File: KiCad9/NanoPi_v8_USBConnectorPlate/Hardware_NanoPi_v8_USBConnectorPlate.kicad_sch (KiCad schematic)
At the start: 17 parts, among them J10 Conn_01x04, J11 Conn_01x02, J12 Conn_01x02, J2 USB_Host_Data_02x02, J3 USB_Host_Data_02x02, J4 USB_Power_02x02, J5 Conn_01x03, J6 Conn_01x09, J8 Conn_01x09, U1 USBLC6-2P6, U2 USBLC6-2P6, U3 USBLC6-2P6

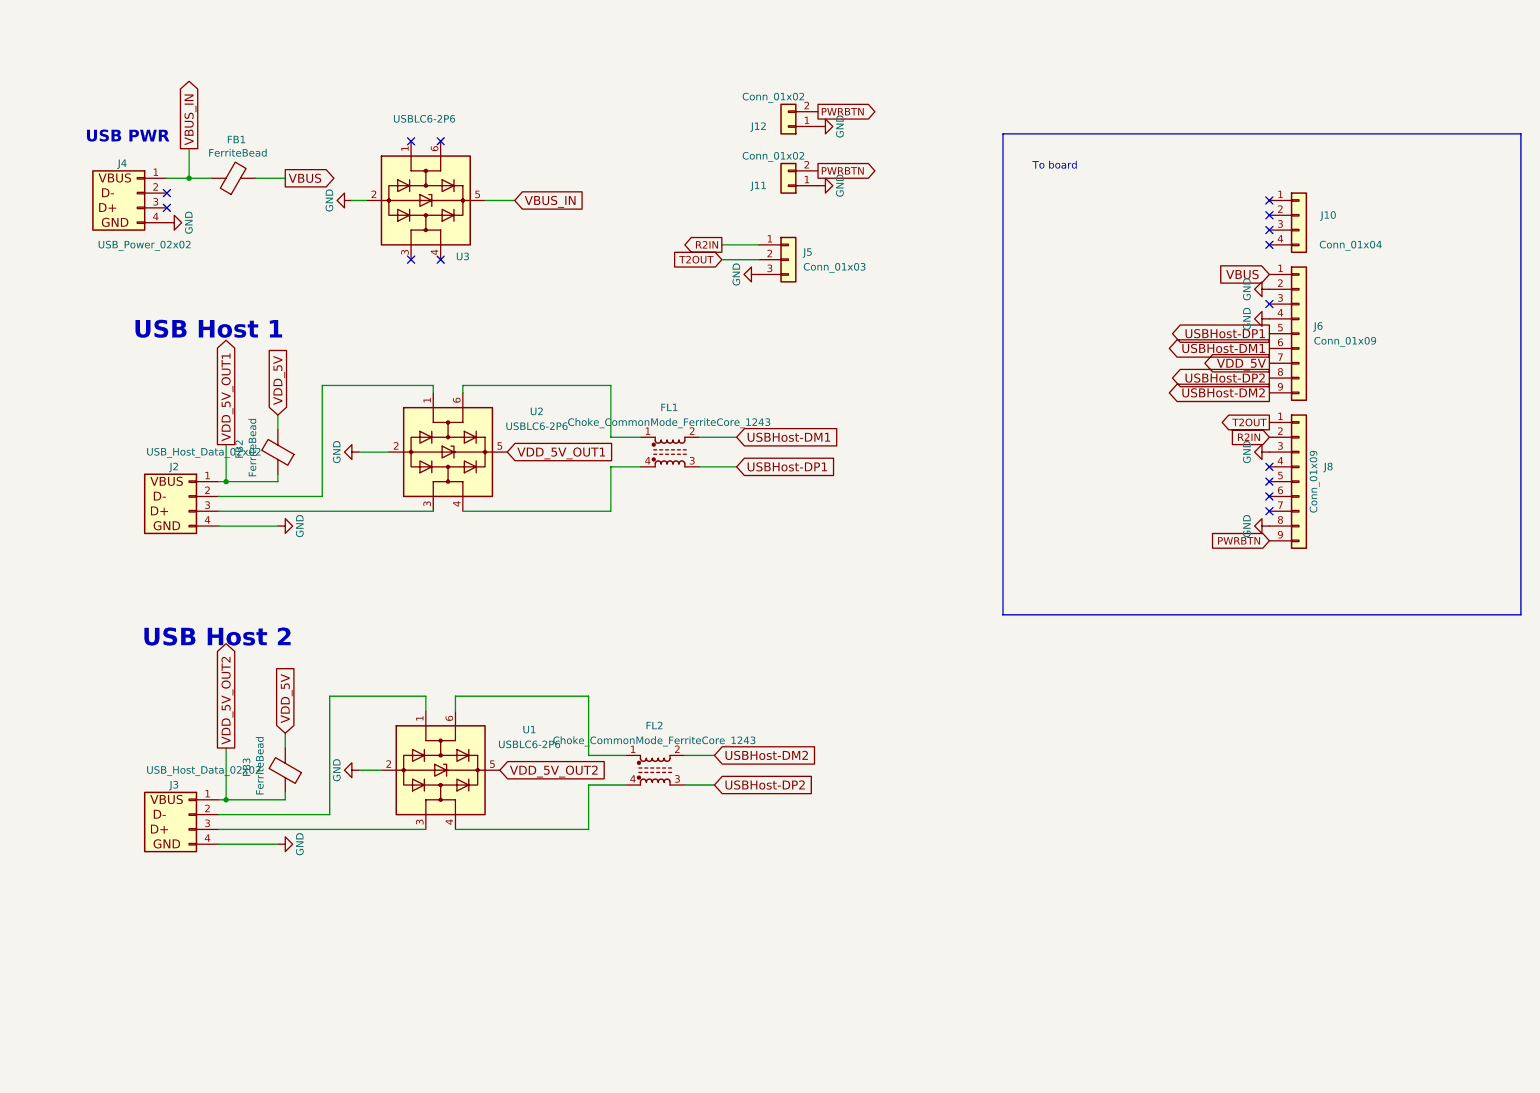
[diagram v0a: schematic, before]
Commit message: add bom
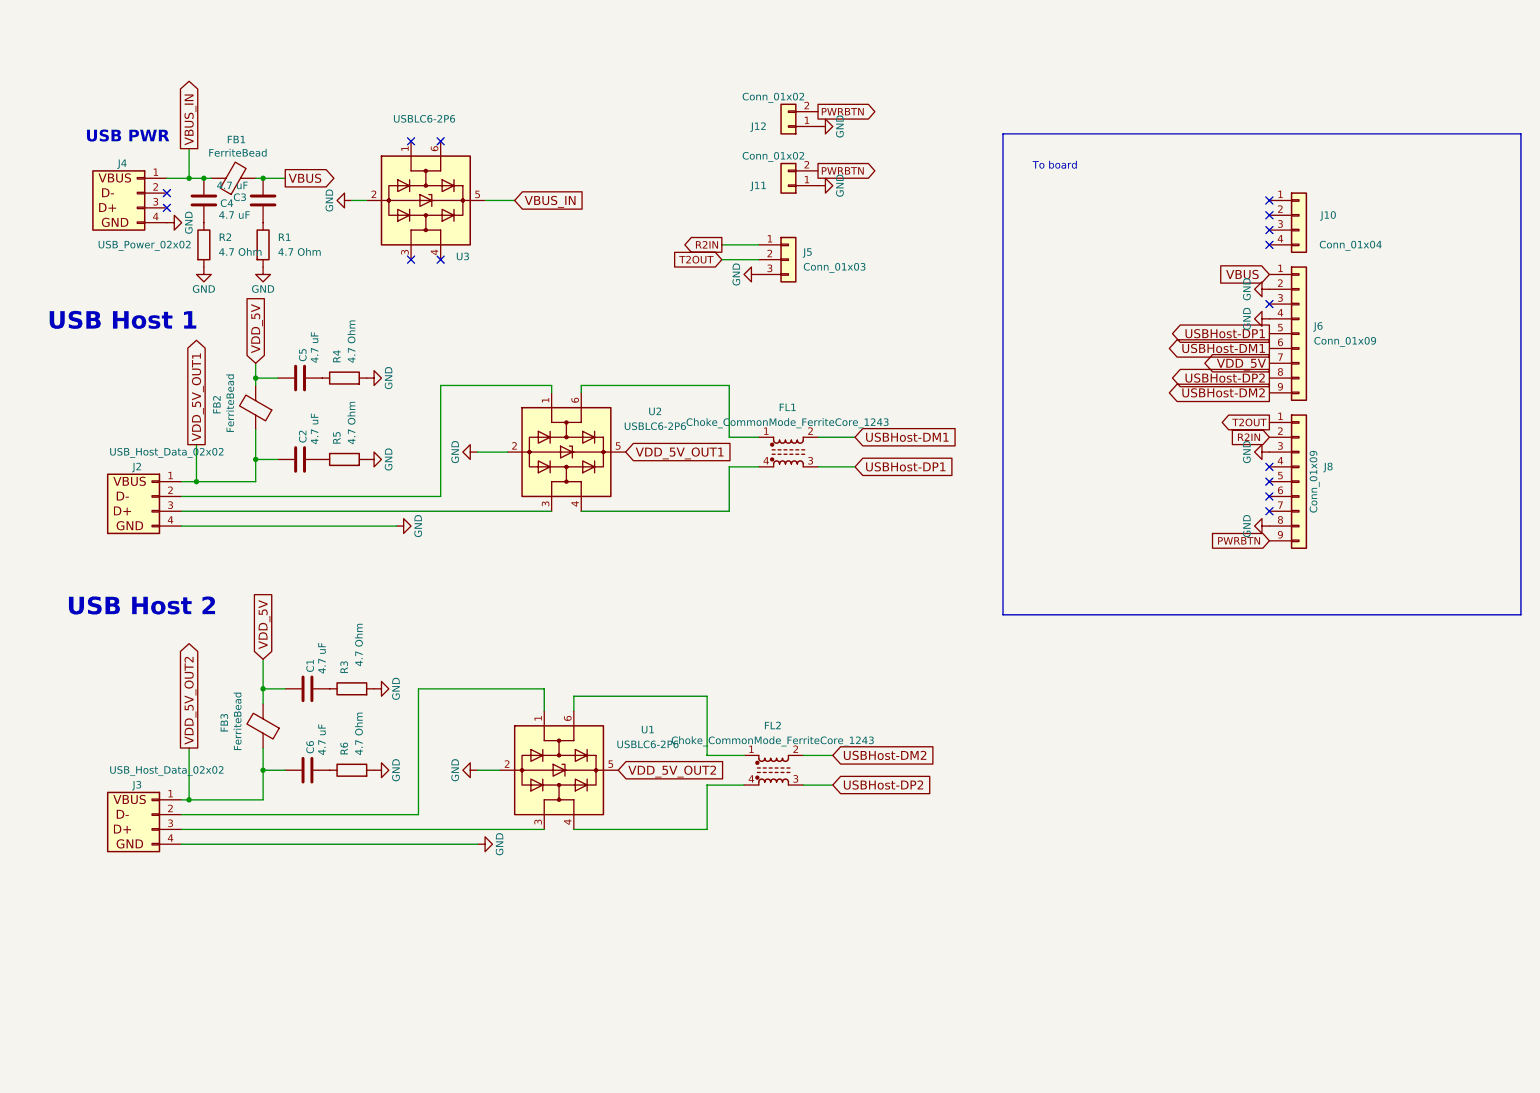
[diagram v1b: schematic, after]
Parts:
- added C1, C2, C3, C4, C5, C6: 4.7 uF, Capacitor_SMD:C_0402_1005Metric, symbol Device:C
- added R1, R2, R3, R4, R5, R6: 4.7 Ohm, Resistor_SMD:R_0603_1608Metric, symbol Device:R
- FB1, FB2: LCSC (none) -> C16902; LCSC Part # (none) -> C16902
- FB3: LCSC (none) -> C16902; LCSC Part # (none) -> C16902; Package (none) -> 1206; PartNumber (none) -> BLM31PG601SN1
- FL1, FL2: LCSC (none) -> C2980700; Package (none) -> SMD-4P,1.2x2mm; PartNumber (none) -> SDCW2012L-2-900TF
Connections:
- net GND: now also R1.2, R2.2, R3.2, R4.2, R5.2, R6.2
- net VBUS: now also C3.2
- net VBUS_IN: now also C4.1
- net VDD_5V: now also C1.1, C5.1
- net VDD_5V_OUT1: now also C2.1
- net VDD_5V_OUT2: now also C6.1
- new net: C5.2, R4.1
- new net: C4.2, R2.1
- new net: C3.1, R1.1
- new net: C1.2, R3.1
- new net: C2.2, R5.1
- new net: C6.2, R6.1
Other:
- moved on the sheet: FB2, FB3, FL1, J2, J3, U1, U2

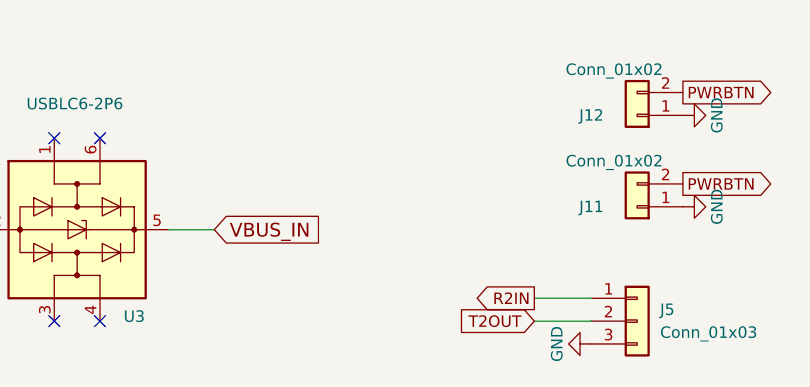
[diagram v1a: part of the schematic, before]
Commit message: add 3d of wifiboard
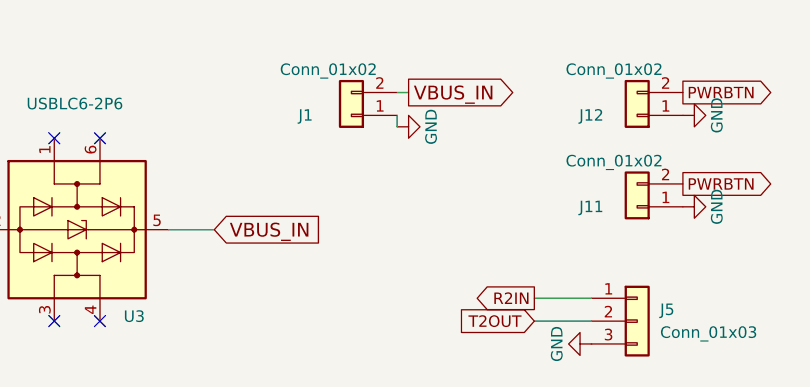
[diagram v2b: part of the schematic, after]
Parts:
- added J1: Conn_01x02, Connector_PinHeader_2.54mm:PinHeader_1x02_P2.54mm_Horizontal, symbol Connector_Generic:Conn_01x02
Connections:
- net GND: now also J1.1 (Pin_1)
- net VBUS_IN: now also J1.2 (Pin_2)
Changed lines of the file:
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@@
 	(wire
 		(pts
+			(xy 115.57 33.02) (xy 115.57 31.75)
+		)
+		(stroke
+			(width 0)
+			(type default)
+		)
+	)
+	(wire
+		(pts
 			(xy 130.81 52.07) (xy 137.16 52.07)
 		)
@@
 	(wire
 		(pts
+			(xy 116.84 29.21) (xy 115.57 29.21)
+		)
+		(stroke
+			(width 0)
+			(type default)
+		)
+	)
+	(wire
+		(pts
 			(xy 130.81 54.61) (xy 137.16 54.61)
 		)
@@
 		)
 	)
+	(global_label "VBUS_IN"
+		(shape output)
+		(at 116.84 29.21 0)
+		(fields_autoplaced yes)
+		(effects
+			(font
+				(size 1.524 1.524)
+			)
+			(justify left)
+		)
+		(property "Intersheetrefs" "${INTERSHEET_REFS}"
+			(at 129.7834 29.21 0)
+			(effects
+				(font
+					(size 1.27 1.27)
+				)
+				(justify left)
+				(hide yes)
+			)
+		)
+	)
 	(global_label "USBHost-DM2"
 		(shape input)
@@
 	(symbol
 		(lib_id "power:GND")
+		(at 115.57 33.02 90)
+		(unit 1)
+		(exclude_from_sim no)
+		(in_bom yes)
+		(on_board yes)
+		(dnp no)
+		(property "Reference" "#PWR020"
+			(at 121.92 33.02 0)
+			(effects
+				(font
+					(size 1.27 1.27)
+				)
+				(hide yes)
+			)
+		)
+		(property "Value" "GND"
+			(at 119.38 33.02 0)
+			(effects
+				(font
+					(size 1.27 1.27)
+				)
+			)
+		)
+		(property "Footprint" ""
+			(at 115.57 33.02 0)
+			(effects
+				(font
+					(size 1.27 1.27)
+				)
+				(hide yes)
+			)
+		)
+		(property "Datasheet" ""
+			(at 115.57 33.02 0)
+			(effects
+				(font
+					(size 1.27 1.27)
+				)
+				(hide yes)
+			)
+		)
+		(property "Description" ""
+			(at 115.57 33.02 0)
+			(effects
+				(font
+					(size 1.27 1.27)
+				)
+				(hide yes)
+			)
+		)
+		(pin "1"
+		)
+		(instances
+			(project "Hardware_NanoPi_v8_USBConnectorPlate"
+				(path "/9af3723b-dbaa-4340-b307-945f921ae404"
+					(reference "#PWR020")
+					(unit 1)
+				)
+			)
+		)
+	)
+	(symbol
+		(lib_id "power:GND")
 		(at 71.12 142.24 90)
 		(unit 1)
@@
 					(unit 1)
 				)
+			)
+		)
+	)
+	(symbol
+		(lib_id "Connector_Generic:Conn_01x02")
+		(at 110.49 31.75 180)
+		(unit 1)
+		(exclude_from_sim no)
+		(in_bom yes)
+		(on_board yes)
+		(dnp no)
+		(property "Reference" "J1"
+			(at 105.41 31.75 0)
+			(effects
+				(font
+					(size 1.27 1.27)
+				)
+			)
+		)
+		(property "Value" "Conn_01x02"
+			(at 107.95 26.67 0)
+			(effects
+				(font
+					(size 1.27 1.27)
+				)
+			)
+		)
+		(property "Footprint" "Connector_PinHeader_2.54mm:PinHeader_1x02_P2.54mm_Horizontal"
+			(at 110.49 31.75 0)
+			(effects
+				(font
+					(size 1.27 1.27)
+				)
+				(hide yes)
+			)
+		)
+		(property "Datasheet" "~"
+			(at 110.49 31.75 0)
+			(effects
+				(font
+					(size 1.27 1.27)
+				)
+				(hide yes)
+			)
+		)
+		(property "Description" ""
+			(at 110.49 31.75 0)
+			(effects
+				(font
+					(size 1.27 1.27)
+				)
+				(hide yes)
+			)
+		)
+		(pin "1"
+		)
+		(pin "2"
+		)
+		(instances
+			(project "Hardware_NanoPi_v8_USBConnectorPlate"
+				(path "/9af3723b-dbaa-4340-b307-945f921ae404"
+					(reference "J1")
+					(unit 1)
+				)

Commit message: etc
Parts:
- removed FL1, FL2: Choke_CommonMode_FerriteCore_1243, WiRoc:0805_CommonModeChoke, symbol Filter:Choke_CommonMode_FerriteCore_1243
- added FL3, FL4: Choke_CommonMode_FerriteCore_1423, WiRoc:0805_CommonModeChoke_1423, symbol Filter:Choke_CommonMode_FerriteCore_1423
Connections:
- net USBHost-DM1: now also FL3.4
- net USBHost-DM2: now also FL4.4
- net USBHost-DP1: now also FL3.3
- net USBHost-DP2: now also FL4.3
- net at U1.6 (I/O1): now also FL4.1
- net at U1.4 (I/O2): now also FL4.2
- net at U2.6 (I/O1): now also FL3.1
- net at U2.4 (I/O2): now also FL3.2
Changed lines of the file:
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@@
 	)
 	(symbol
-		(lib_id "Filter:Choke_CommonMode_FerriteCore_1243")
-		(at 139.7 142.24 0)
-		(unit 1)
-		(exclude_from_sim no)
-		(in_bom yes)
-		(on_board yes)
-		(dnp no)
-		(fields_autoplaced yes)
-		(property "Reference" "FL2"
-			(at 139.573 134.62 0)
-			(effects
-				(font
-					(size 1.27 1.27)
-				)
-			)
-		)
-		(property "Value" "Choke_CommonMode_FerriteCore_1243"
-			(at 139.573 137.16 0)
-			(effects
-				(font
-					(size 1.27 1.27)
-				)
-			)
-		)
-		(property "Footprint" "WiRoc:0805_CommonModeChoke"
-			(at 139.7 148.59 0)
-			(effects
-				(font
-					(size 1.27 1.27)
-				)
-				(hide yes)
-			)
-		)
-		(property "Datasheet" "https://jlcpcb.com/api/file/downloadByFileSystemAccessId/8590903681308958720"
-			(at 139.7 150.495 0)
-			(effects
-				(font
-					(size 1.27 1.27)
-				)
-				(hide yes)
-			)
-		)
-		(property "Description" "Generic common-mode choke, ferrite core, 1243 pin order"
-			(at 143.764 143.002 0)
-			(effects
-				(font
-					(size 1.27 1.27)
-				)
-				(hide yes)
-			)
-		)
-		(property "PartNumber" "SDCW2012L-2-900TF"
-			(at 139.7 142.24 0)
-			(effects
-				(font
-					(size 1.27 1.27)
-				)
-				(hide yes)
-			)
-		)
-		(property "LCSC" "C2980700"
-			(at 139.7 142.24 0)
-			(effects
-				(font
-					(size 1.27 1.27)
-				)
-				(hide yes)
-			)
-		)
-		(property "Package" "SMD-4P,1.2x2mm"
-			(at 139.7 142.24 0)
-			(effects
-				(font
-					(size 1.27 1.27)
-				)
-				(hide yes)
-			)
-		)
-		(pin "4"
-		)
-		(pin "2"
-		)
-		(pin "1"
-		)
-		(pin "3"
-		)
-		(instances
-			(project "Hardware_NanoPi_v8_USBConnectorPlate"
-				(path "/9af3723b-dbaa-4340-b307-945f921ae404"
-					(reference "FL2")
-					(unit 1)
-				)
-			)
-		)
-	)
-	(symbol
 		(lib_id "Connector_Generic:Conn_01x03")
 		(at 142.24 54.61 0)
@@
 	)
 	(symbol
-		(lib_id "Filter:Choke_CommonMode_FerriteCore_1243")
-		(at 142.24 87.63 0)
-		(unit 1)
-		(exclude_from_sim no)
-		(in_bom yes)
-		(on_board yes)
-		(dnp no)
-		(fields_autoplaced yes)
-		(property "Reference" "FL1"
-			(at 142.113 80.01 0)
-			(effects
-				(font
-					(size 1.27 1.27)
-				)
-			)
-		)
-		(property "Value" "Choke_CommonMode_FerriteCore_1243"
-			(at 142.113 82.55 0)
-			(effects
-				(font
-					(size 1.27 1.27)
-				)
-			)
-		)
-		(property "Footprint" "WiRoc:0805_CommonModeChoke"
-			(at 142.24 93.98 0)
-			(effects
-				(font
-					(size 1.27 1.27)
-				)
-				(hide yes)
-			)
-		)
-		(property "Datasheet" "https://jlcpcb.com/api/file/downloadByFileSystemAccessId/8590903681308958720"
-			(at 142.24 95.885 0)
-			(effects
-				(font
-					(size 1.27 1.27)
-				)
-				(hide yes)
-			)
-		)
-		(property "Description" "Generic common-mode choke, ferrite core, 1243 pin order"
-			(at 146.304 88.392 0)
-			(effects
-				(font
-					(size 1.27 1.27)
-				)
-				(hide yes)
-			)
-		)
-		(property "PartNumber" "SDCW2012L-2-900TF"
-			(at 142.24 87.63 0)
-			(effects
-				(font
-					(size 1.27 1.27)
-				)
-				(hide yes)
-			)
-		)
-		(property "LCSC" "C2980700"
-			(at 142.24 87.63 0)
-			(effects
-				(font
-					(size 1.27 1.27)
-				)
-				(hide yes)
-			)
-		)
-		(property "Package" "SMD-4P,1.2x2mm"
-			(at 142.24 87.63 0)
-			(effects
-				(font
-					(size 1.27 1.27)
-				)
-				(hide yes)
-			)
-		)
-		(pin "4"
-		)
-		(pin "2"
-		)
-		(pin "1"
-		)
-		(pin "3"
-		)
-		(instances
-			(project ""
-				(path "/9af3723b-dbaa-4340-b307-945f921ae404"
-					(reference "FL1")
-					(unit 1)
-				)
-			)
-		)
-	)
-	(symbol
 		(lib_id "power:GND")
 		(at 41.91 55.88 0)
@@
 	)
 	(symbol
+		(lib_id "Filter:Choke_CommonMode_FerriteCore_1423")
+		(at 139.7 142.24 0)
+		(unit 1)
+		(exclude_from_sim no)
+		(in_bom yes)
+		(on_board yes)
+		(dnp no)
+		(fields_autoplaced yes)
+		(property "Reference" "FL4"
+			(at 139.573 134.62 0)
+			(effects
+				(font
+					(size 1.27 1.27)
+				)
+			)
+		)
+		(property "Value" "Choke_CommonMode_FerriteCore_1423"
+			(at 139.573 137.16 0)
+			(effects
+				(font
+					(size 1.27 1.27)
+				)
+			)
+		)
+		(property "Footprint" "WiRoc:0805_CommonModeChoke_1423"
+			(at 139.7 148.59 0)
+			(effects
+				(font
+					(size 1.27 1.27)
+				)
+				(hide yes)
+			)
+		)
+		(property "Datasheet" "~"
+			(at 139.7 150.495 0)
+			(effects
+				(font
+					(size 1.27 1.27)
+				)
+				(hide yes)
+			)
+		)
+		(property "Description" "Generic common-mode choke, ferrite core, 1423 pin order"
+			(at 139.7 142.24 0)
+			(effects
+				(font
+					(size 1.27 1.27)
+				)
+				(hide yes)
+			)
+		)
+		(property "LCSC" "C49023314"
+			(at 139.7 142.24 0)
+			(effects
+				(font
+					(size 1.27 1.27)
+				)
+				(hide yes)
+			)
+		)
+		(property "LCSC Part #" "C49023314"
+			(at 139.7 142.24 0)
+			(effects
+				(font
+					(size 1.27 1.27)
+				)
+				(hide yes)
+			)
+		)
+		(pin "4"
+		)
+		(pin "1"
+		)
+		(pin "2"
+		)
+		(pin "3"
+		)
+		(instances
+			(project "Hardware_NanoPi_v8_USBConnectorPlate"
+				(path "/9af3723b-dbaa-4340-b307-945f921ae404"
+					(reference "FL4")
+					(unit 1)
+				)
+			)
+		)
+	)
+	(symbol
 		(lib_id "power:GND")
 		(at 69.85 88.9 90)
@@
 					(unit 1)
 				)
+			)
+		)
+	)
+	(symbol
+		(lib_id "Filter:Choke_CommonMode_FerriteCore_1423")
+		(at 142.24 87.63 0)
+		(unit 1)
+		(exclude_from_sim no)
+		(in_bom yes)
+		(on_board yes)
+		(dnp no)
+		(fields_autoplaced yes)
+		(property "Reference" "FL3"
+			(at 142.113 80.01 0)
+			(effects
+				(font
+					(size 1.27 1.27)
+				)
+			)
+		)
+		(property "Value" "Choke_CommonMode_FerriteCore_1423"
+			(at 142.113 82.55 0)
+			(effects
+				(font
+					(size 1.27 1.27)
+				)
+			)
+		)
+		(property "Footprint" "WiRoc:0805_CommonModeChoke_1423"
+			(at 142.24 93.98 0)
+			(effects
+				(font
+					(size 1.27 1.27)
+				)
+				(hide yes)
+			)
+		)
+		(property "Datasheet" "~"
+			(at 142.24 95.885 0)
+			(effects
+				(font
+					(size 1.27 1.27)
+				)
+				(hide yes)
+			)
+		)
+		(property "Description" "Generic common-mode choke, ferrite core, 1423 pin order"
+			(at 142.24 87.63 0)
+			(effects
+				(font
+					(size 1.27 1.27)
+				)
+				(hide yes)
+			)
+		)
+		(property "LCSC" "C49023314"
+			(at 142.24 87.63 0)
+			(effects
+				(font
+					(size 1.27 1.27)
+				)
+				(hide yes)
+			)
+		)
+		(property "LCSC Part #" "C49023314"
+			(at 142.24 87.63 0)
+			(effects
+				(font
+					(size 1.27 1.27)
+				)
+				(hide yes)
+			)
+		)
+		(pin "4"
+		)
+		(pin "1"
+		)
+		(pin "2"
+		)
+		(pin "3"
+		)
+		(instances
+			(project ""
+				(path "/9af3723b-dbaa-4340-b307-945f921ae404"
+					(reference "FL3")
+					(unit 1)
+				)

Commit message: add ethernet etc
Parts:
- removed J5: Conn_01x03, WiRoc:SerialConnPads3Pin, symbol Connector_Generic:Conn_01x03
- added C10, C11, C12, C13, C7, C8, C9: 100 nF, Capacitor_SMD:C_0402_1005Metric, symbol Device:C
- added C14: 1 nF 2kV, Capacitor_SMD:C_1206_3216Metric, symbol Device:C
- added FB4: FerriteBead, Inductor_SMD:L_1206_3216Metric, symbol Device:FerriteBead
- added FL1, FL2: MCZ1210AH900L2TA0G, WiRoc:MCZ1210AH_L2_TDK, symbol Filter:Choke_CommonMode_FerriteCore_1324
- added J5: Conn_01x05, WiRoc:SerialAndEthConnPads4Pin, symbol Connector_Generic:Conn_01x05
- added NT1, NT2: NetTie_2, WiRoc:NetTie-2_SMD_Pad0.3mm, symbol Device:NetTie_2
- added R7, R8: 75 Ohm, Resistor_SMD:R_0603_1608Metric, symbol Device:R
- added U4, U5: ALT4532M-201-T001, WiRoc:ALT4532M_TDK, symbol ALT4532M:ALT4532M-201-T001
- added U8: SP3232ECY-L, WiRoc:TSSOP-16_4.4x5mm_P0.65mm_PartOfSilkscreenRemoved, symbol Interface_UART:MAX3232
- C1, C2, C3, C4, C5, C6, R1, R2, R3, R4, R5, R6: JLCPCBBasic (none) -> YES
- FB1, FB2, FB3, FL3, FL4: JLCPCBBasic (none) -> NO
- J1, J10, J11, J12, J6, J8: now not fitted
- U1, U2, U3: JLCPCBBasic (none) -> NO; LCSC (none) -> C15999; LCSC Part # (none) -> C15999
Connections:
- net GND: now also C10.1, C11.1, C12.1, C13.1, C8.1, FB4.1, J5.3 (Pin_3), U8.15 (GND); no longer J8.8 (Pin_8)
- net R2IN: now also U8.9 (R2OUT)
- net T2OUT: now also U8.10 (T2IN)
- net EPHY-RXP: now reaches J8.4 (Pin_4)
- net EPHY-RXP: now also U4.2
- net EPHY-RXN: now reaches J8.5 (Pin_5)
- net EPHY-RXN: now also U4.1
- net EPHY-TXP: now reaches J8.6 (Pin_6)
- net EPHY-TXP: now also U5.1
- net EPHY-TXN: now reaches J8.7 (Pin_7)
- net EPHY-TXN: now also U5.2
- new net: C13.2, U4.3
- new net: R7.1, U4.6
- new net: C11.2, U8.6 (VS-)
- new net: C14.1, R7.2, R8.2
- new net: C14.2, FB4.2
- new net: C9.1, U8.4 (C2+)
- new net: C9.2, U8.5 (C2-)
- new net: C7.1, U8.1 (C1+)
- new net: C7.2, U8.3 (C1-)
- new net: C10.2, U8.2 (VS+)
- new net: C12.2, U5.3
- new net: R8.1, U5.6
- new net CABLE-RXN: FL2.4, NT2.1
- new net CABLE-RXP: FL2.3, J5.5 (Pin_5)
- new net CABLE-TXN: FL1.3, NT1.1
- new net CABLE-TXP: FL1.4, J5.4 (Pin_4)
- new net ETH-RXN: FL1.2, U5.5
- new net ETH-RXP: FL1.1, U5.4
- new net ETH-TXN: FL2.2, U4.5
- new net ETH-TXP: FL2.1, U4.4
- new net SYS_3.3V: C8.2, J8.8 (Pin_8), U8.16 (VCC)
- new net UART2_RX: J5.1 (Pin_1), NT1.2, U8.8 (R2IN)
- new net UART2_TX: J5.2 (Pin_2), NT2.2, U8.7 (T2OUT)
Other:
- note added: "Ethernet"
- moved on the sheet: C1, C2, C3, C4, C5, C6, FB1, FB2, FB3, FL3, FL4, J2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
